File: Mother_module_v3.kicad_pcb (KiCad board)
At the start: 4 copper layers, 86.5 x 67.8 mm, 2 parts, among them U1 Virtual_Digital_module_v3, U3 Power_manager_v3

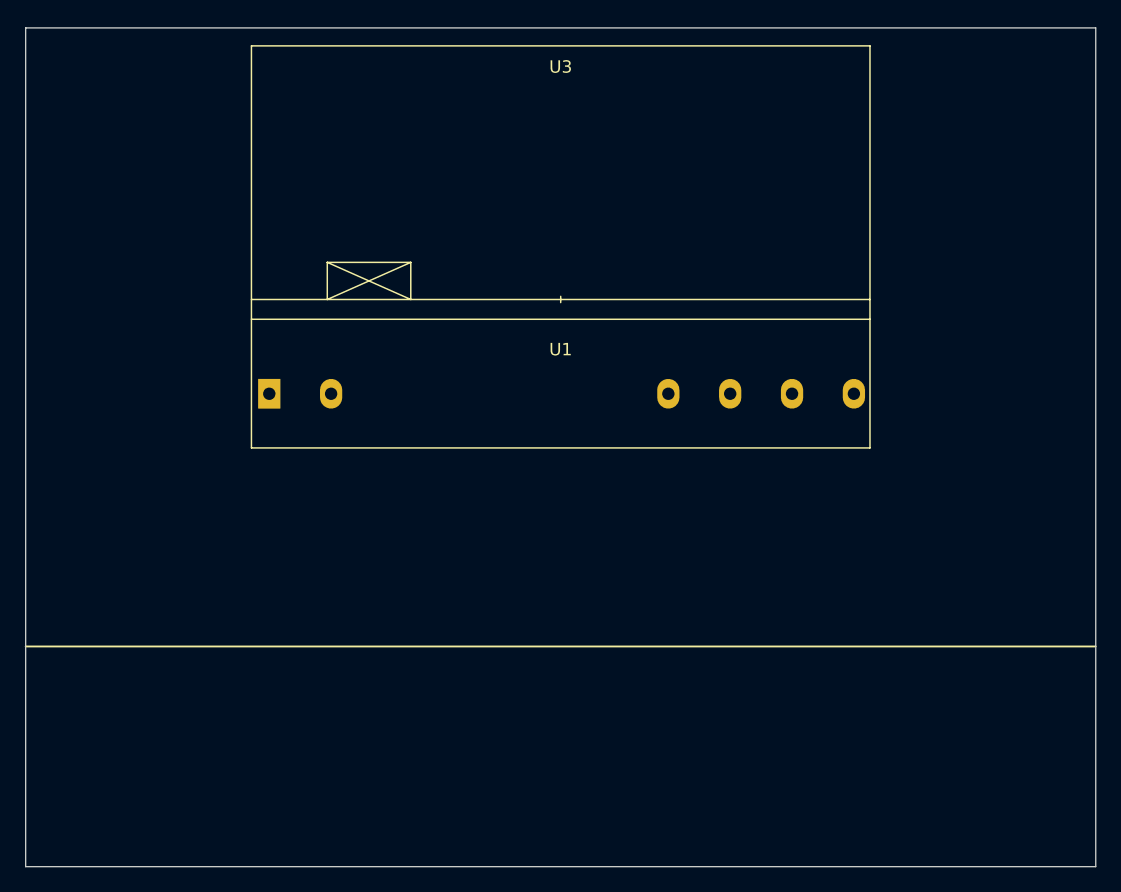
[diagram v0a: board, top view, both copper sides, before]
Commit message: Исправления в схеме и в печатной плате. Размещены два модуля.
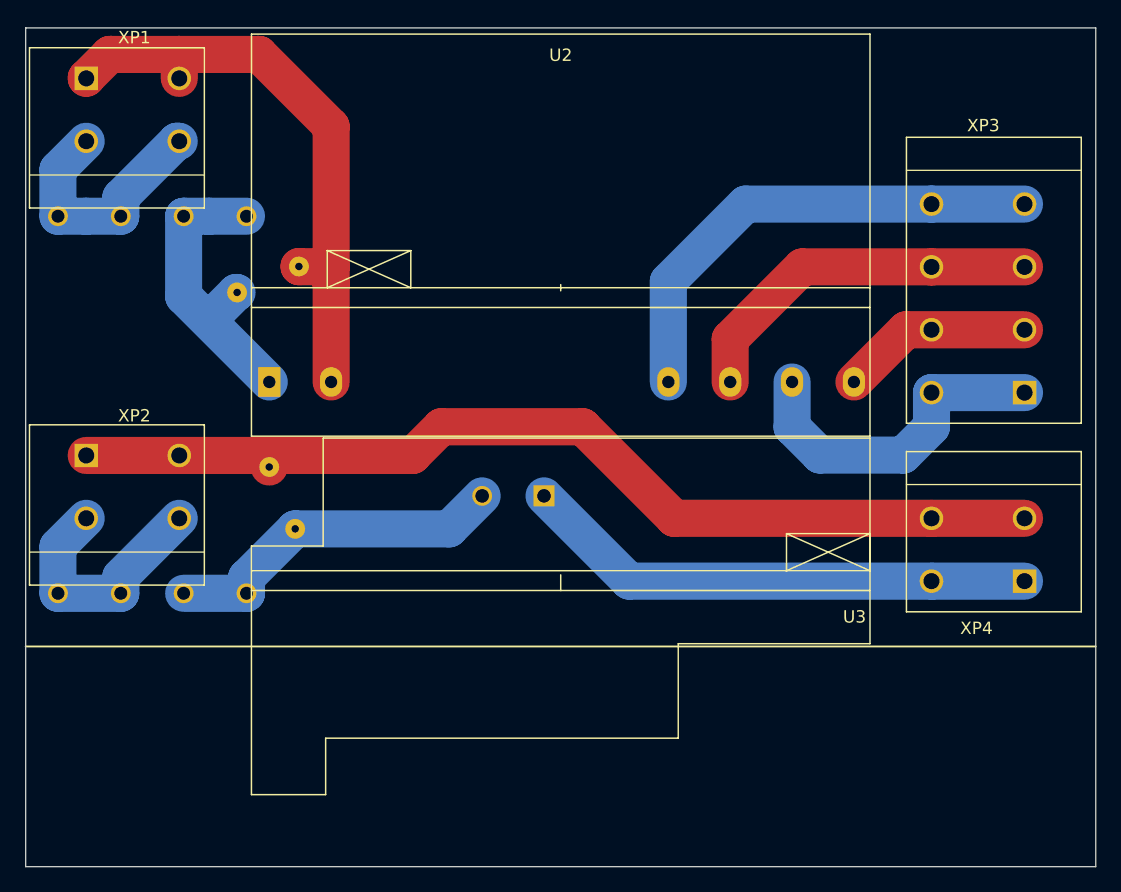
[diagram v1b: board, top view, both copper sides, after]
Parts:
- removed U1: Virtual_Digital_module_v3, Modules:Virtual_Digital_module_v3
- added F1: 0.5A, Modules:FC-05C-E_4x15, B.Cu at (74.6, 90.2)
- added F2: 0.5A, Modules:FC-05C-E_4x15, B.Cu at (74.6, 120.7)
- added RV1: 470V, Varistor:RV_Disc_D7mm_W4.5mm_P5mm, B.Cu at (73.8, 96.4)
- added RV2: 470V, Varistor:RV_Disc_D7mm_W4.5mm_P5mm, B.Cu at (78.5, 115.5)
- added U3: Fan_control_module_v3, Modules:Fan_controller_v3, F.Cu at (100.0, 120.5)
- added XP1: ACin, Modules:XY122R-5.08-02P-14, F.Cu at (61.6, 79.1)
- added XP2: ACin, Modules:XY122R-5.08-02P-14, F.Cu at (61.6, 109.6)
- added XP3: LoadX, Modules:XY122R-5.08-04P-14, F.Cu at (137.5, 104.5)
- added XP4: LoadX, Modules:XY122R-5.08-02P-14, F.Cu at (137.5, 119.7)
- U2: renamed from U3; value Power_manager_v3 -> Power_manager_v3-Modules
- moved U2 0.95 mm to (100.0, 96.0)
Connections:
- U2 pad 2: /N1 -> Net-(RV1-Pad2)
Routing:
- net Net-(RV2-Pad2): track 0.00 -> 80.8 mm
- net Net-(RV1-Pad2): track 0.00 -> 48.3 mm
- net Net-(U3-Pad1): track 0.00 -> 41.6 mm
- net Net-(U2-Pad3): track 0.00 -> 39.5 mm
- net Net-(U2-Pad4): track 0.00 -> 29.7 mm
- net Net-(F2-Pad1): track 0.00 -> 28.1 mm
- net Net-(U2-Pad5): track 0.00 -> 27.1 mm
- net Net-(F1-Pad1): track 0.00 -> 24.6 mm
- net Net-(F1-Pad2): track 0.00 -> 20.2 mm
- net Net-(F2-Pad2): track 0.00 -> 20.1 mm
- net Net-(U2-Pad6): track 0.00 -> 15.5 mm
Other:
- copper layers 4 -> 2

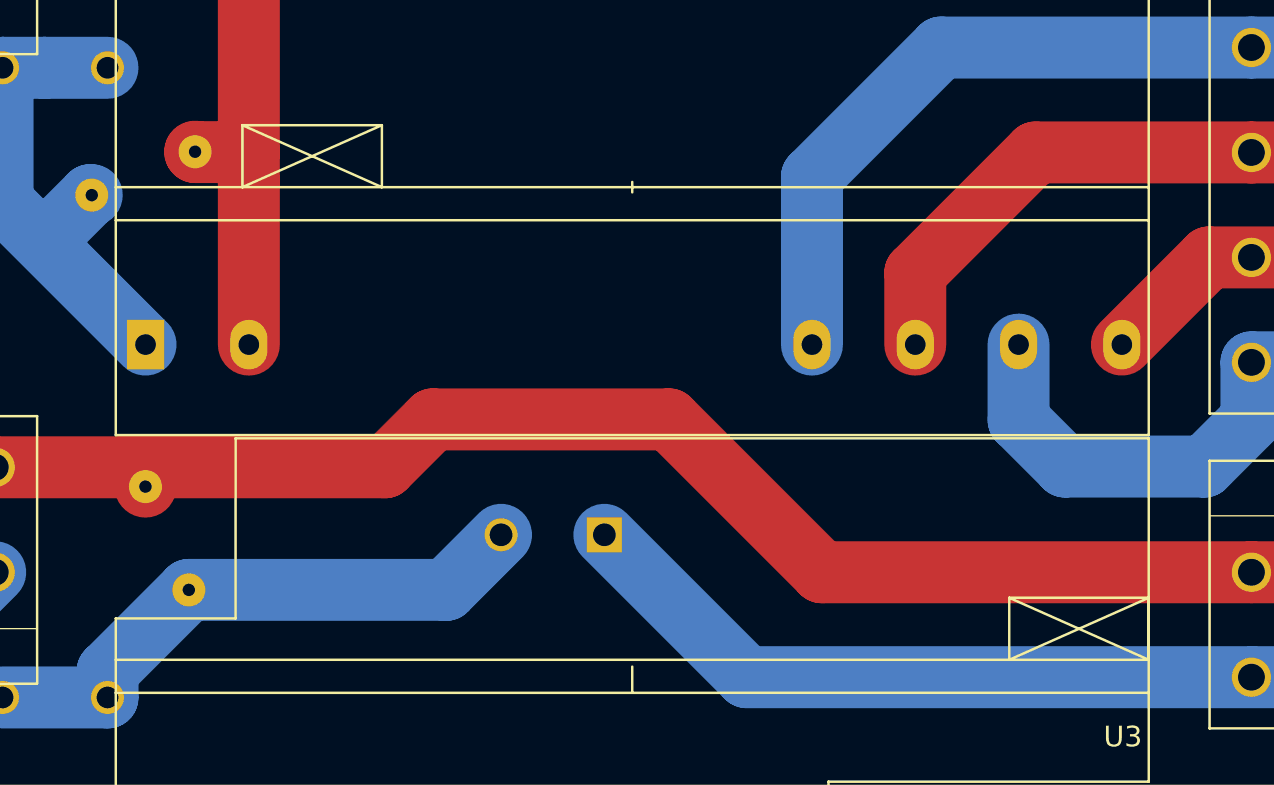
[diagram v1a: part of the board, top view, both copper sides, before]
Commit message: Подправлено положение разъемов и плат модулей.
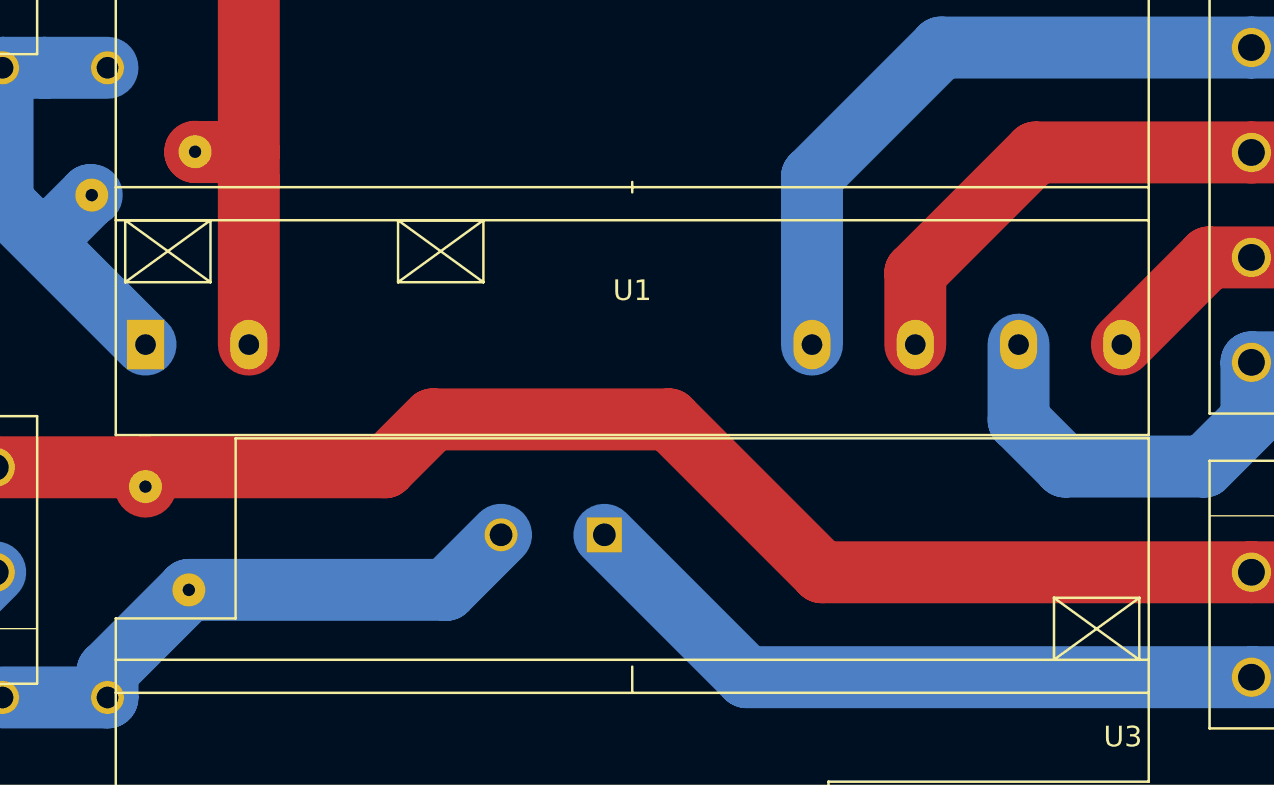
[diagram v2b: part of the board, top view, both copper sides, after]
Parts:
- added U1: Virtual_Digital_module_v3, Modules:Virtual_Digital_module_v3, F.Cu at (100.0, 100.0)
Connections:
- U2 pad 1: Net-(F1-Pad1) -> (no net)
- U2 pad 2: Net-(RV1-Pad2) -> (no net)
- U2 pad 3: Net-(U2-Pad3) -> (no net)
- U2 pad 4: Net-(U2-Pad4) -> (no net)
- U2 pad 5: Net-(U2-Pad5) -> (no net)
- U2 pad 6: Net-(U2-Pad6) -> (no net)
- U3 pad 1: Net-(U3-Pad1) -> (no net)
- U3 pad 2: Net-(F2-Pad1) -> (no net)
